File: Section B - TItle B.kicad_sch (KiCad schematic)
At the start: 12 parts, among them J2 CE, J3 Conn_01x03_Pin, U2 TLV73333PDBV, U3 MSPM0C1104SDSGR

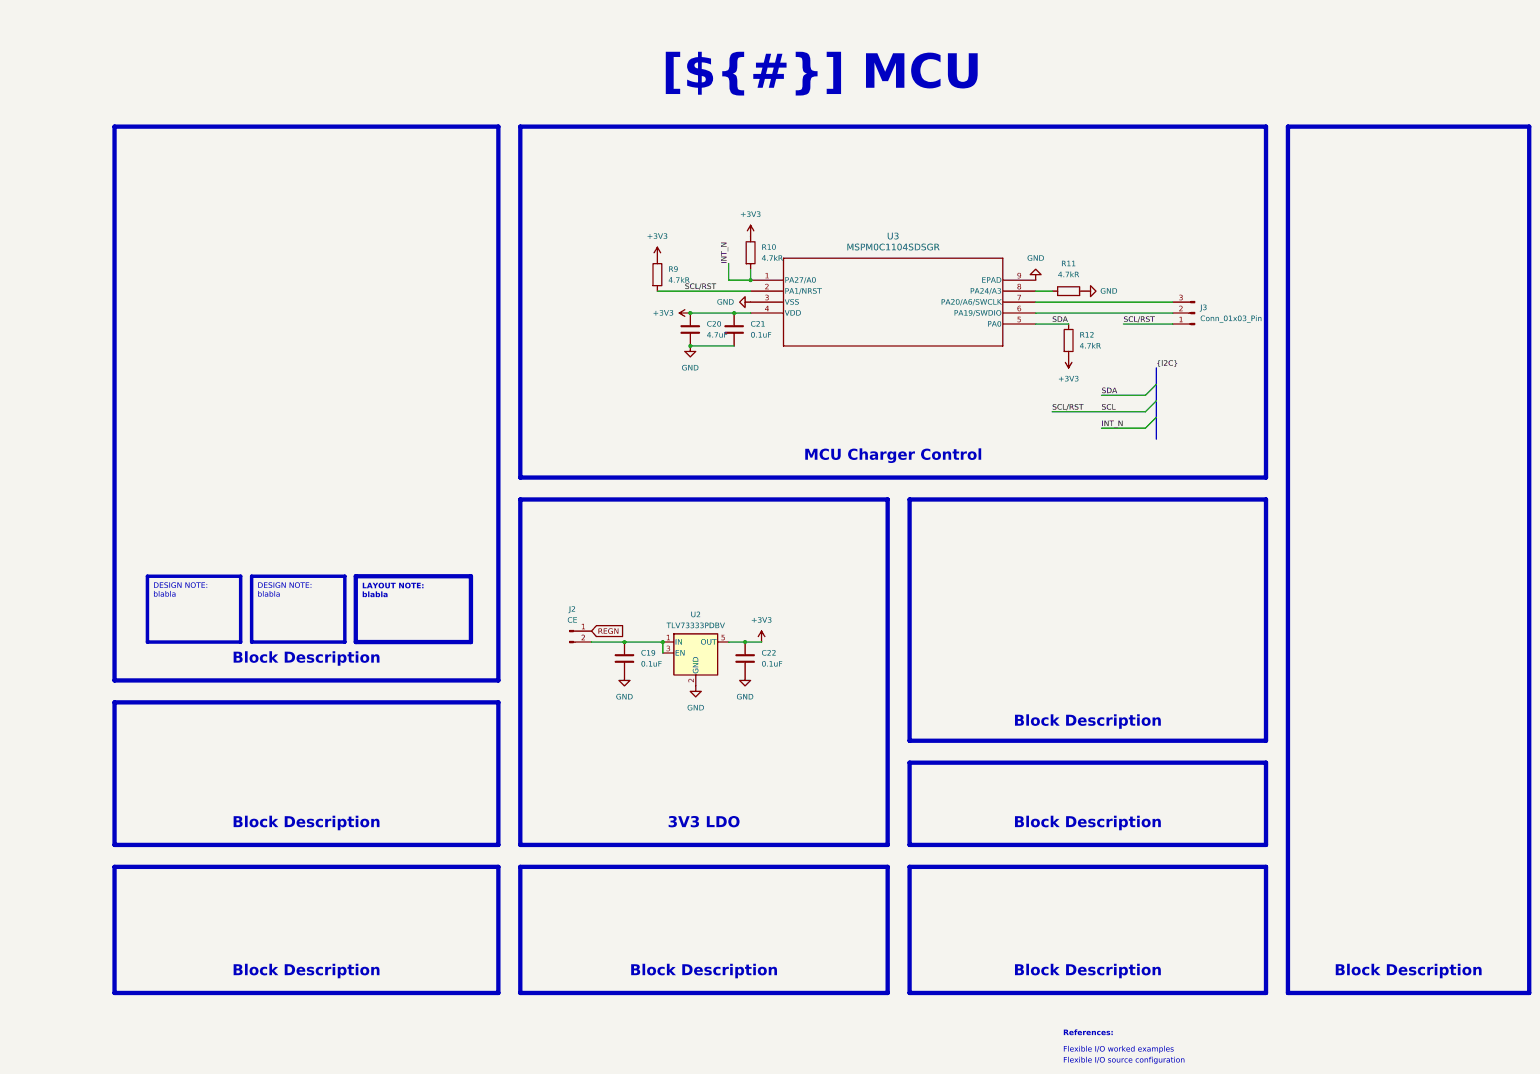
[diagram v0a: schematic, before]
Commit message: Change schematic sheet size to A4
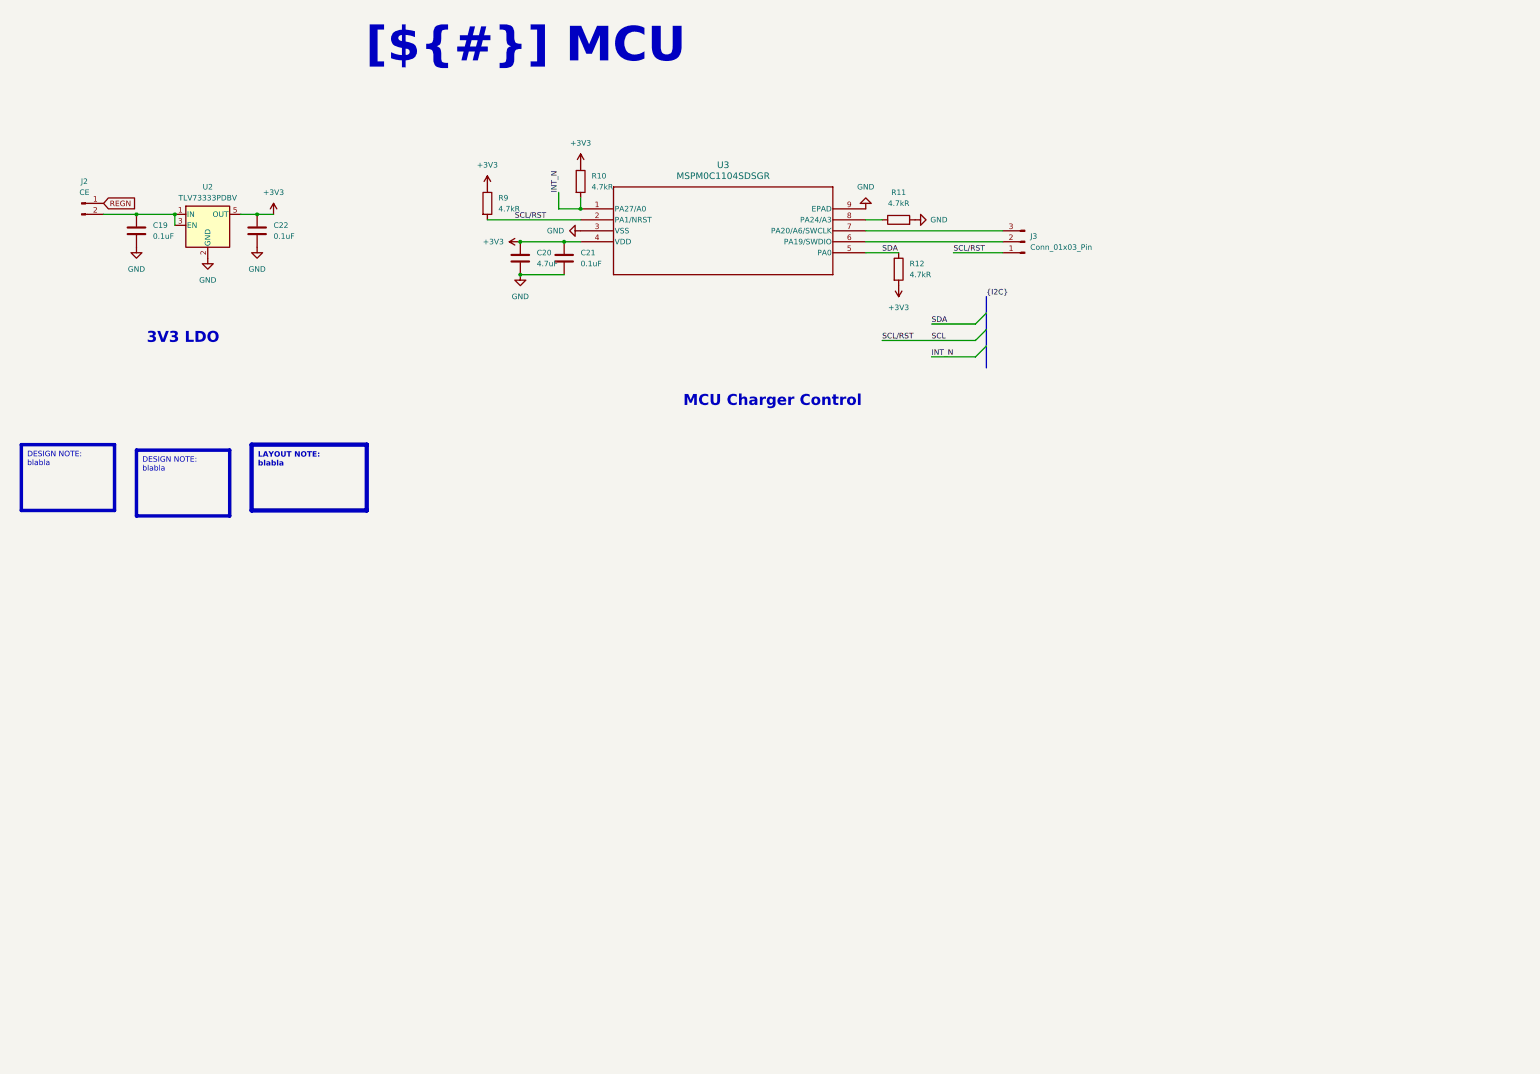
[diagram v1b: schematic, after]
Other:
- note removed: "Flexible I/O source configuration"
- note removed: "Flexible I/O worked examples"
- note removed: "References:"
- moved on the sheet: C19, C20, C21, C22, J2, J3, R10, R11, R12, R9, U2, U3

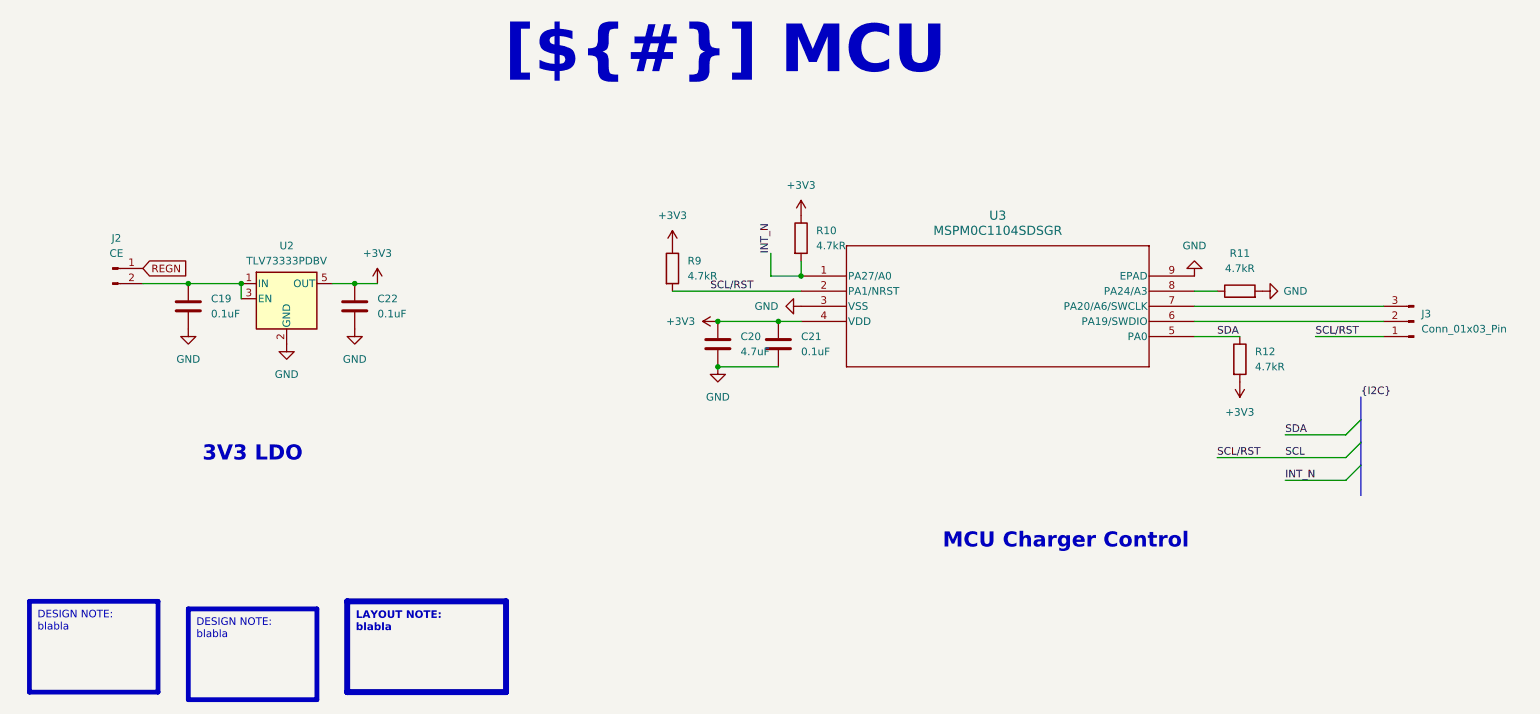
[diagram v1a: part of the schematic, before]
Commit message: Finish schematic
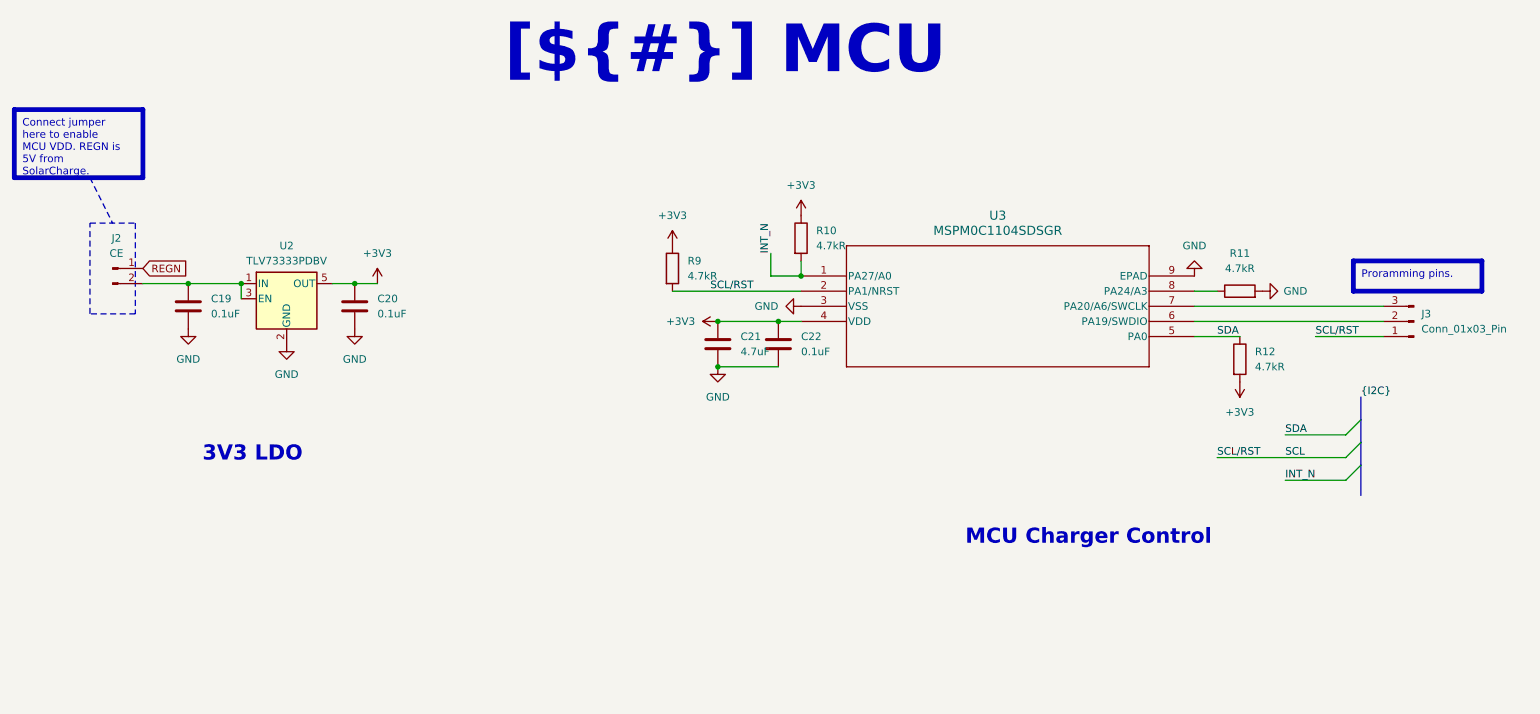
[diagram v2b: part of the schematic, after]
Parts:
- renumbered C22 to C20, C20 to C21, C21 to C22
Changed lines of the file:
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@@
 		(company "${COMPANY}")
+	)
+	(rectangle
+		(start 34.29 49.53)
+		(end 41.91 64.77)
+		(stroke
+			(width 0)
+			(type dot)
+			(color 255 0 0 1)
+		)
+		(fill
+			(type none)
+		)
+	)
+	(text_box "Connect jumper here to enable MCU VDD. REGN is 5V from SolarCharge."
+		(exclude_from_sim no)
+		(at 21.59 30.48 0)
+		(size 21.59 11.43)
+		(margins 1.3525 1.3525 1.3525 1.3525)
+		(stroke
+			(width 0.8)
+			(type solid)
+			(color 250 236 0 1)
+		)
+		(fill
+			(type none)
+		)
+		(effects
+			(font
+				(face "Arial")
+				(size 1.27 1.27)
+				(color 0 0 0 1)
+			)
+			(justify left top)
+		)
 	)
 	(text_box "[${#}] ${TITLE}"
@@
 		)
 	)
-	(text_box "DESIGN NOTE:\nblabla"
-		(exclude_from_sim no)
-		(at 50.8 114.3 0)
-		(size 21.59 15.24)
-		(margins 1.3525 1.3525 1.3525 1.3525)
-		(stroke
-			(width 0.8)
-			(type solid)
-			(color 255 165 0 1)
-		)
-		(fill
-			(type none)
-		)
-		(effects
-			(font
-				(face "Arial")
-				(size 1.27 1.27)
-				(color 0 0 0 1)
-			)
-			(justify left top)
-		)
-	)
-	(text_box "LAYOUT NOTE:\nblabla"
-		(exclude_from_sim no)
-		(at 77.47 113.03 0)
-		(size 26.67 15.24)
-		(margins 1.4525 1.4525 1.4525 1.4525)
-		(stroke
-			(width 1)
-			(type solid)
-			(color 0 0 255 1)
-		)
-		(fill
-			(type none)
-		)
-		(effects
-			(font
-				(face "Arial")
-				(size 1.27 1.27)
-				(thickness 0.4)
-				(bold yes)
-				(color 0 0 255 1)
-			)
-			(justify left top)
-		)
-	)
 	(text_box "MCU Charger Control"
 		(exclude_from_sim no)
-		(at 114.3 96.52 0)
-		(size 167.64 9.525)
+		(at 124.46 95.885 0)
+		(size 154.94 9.525)
 		(margins 1.9049 1.9049 1.9049 1.9049)
 		(stroke
@@
 		)
 	)
-	(text_box "DESIGN NOTE:\nblabla"
-		(exclude_from_sim no)
-		(at 24.13 113.03 0)
-		(size 21.59 15.24)
-		(margins 1.3525 1.3525 1.3525 1.3525)
-		(stroke
-			(width 0.8)
-			(type solid)
-			(color 200 200 200 1)
-		)
-		(fill
-			(type none)
-		)
-		(effects
-			(font
-				(face "Arial")
-				(size 1.27 1.27)
-				(color 0 0 0 1)
-			)
-			(justify left top)
-		)
-	)
 	(text_box "3V3 LDO"
 		(exclude_from_sim no)
@@
 		)
 	)
+	(text_box "Proramming pins."
+		(exclude_from_sim no)
+		(at 246.38 55.88 0)
+		(size 21.59 5.08)
+		(margins 1.3525 1.3525 1.3525 1.3525)
+		(stroke
+			(width 0.8)
+			(type solid)
+			(color 250 236 0 1)
+		)
+		(fill
+			(type none)
+		)
+		(effects
+			(font
+				(face "Arial")
+				(size 1.27 1.27)
+				(color 0 0 0 1)
+			)
+			(justify left top)
+		)
+	)
 	(junction
 		(at 78.74 59.69)
@@
 			(width 0)
 			(type default)
+		)
+	)
+	(polyline
+		(pts
+			(xy 34.29 41.91) (xy 38.1 49.53)
+		)
+		(stroke
+			(width 0)
+			(type dot)
+			(color 255 0 0 1)
 		)
 	)
@@
 		(dnp no)
 		(fields_autoplaced yes)
-		(property "Reference" "#PWR020"
+		(property "Reference" "#PWR023"
 			(at 139.7 80.01 0)
 			(effects
@@
 			(project "solar_smart_station"
 				(path "/f9e05184-c88b-4a88-ae9c-ab2bdb32be7c/c5103ceb-5325-4a84-a025-9638a412984e/e744f3ce-03a6-44a6-8792-1447ef232b9a"
-					(reference "#PWR020")
+					(reference "#PWR023")
 					(unit 1)
 				)
@@
 		(dnp no)
 		(fields_autoplaced yes)
-		(property "Reference" "C21"
+		(property "Reference" "C22"
 			(at 153.67 68.5799 0)
 			(effects
@@
 			(project "solar_smart_station"
 				(path "/f9e05184-c88b-4a88-ae9c-ab2bdb32be7c/c5103ceb-5325-4a84-a025-9638a412984e/e744f3ce-03a6-44a6-8792-1447ef232b9a"
-					(reference "C21")
+					(reference "C22")
 					(unit 1)
 				)
@@
 		(dnp no)
 		(fields_autoplaced yes)
-		(property "Reference" "#PWR025"
+		(property "Reference" "#PWR020"
 			(at 82.55 63.5 0)
 			(effects
@@
 			(project "solar_smart_station"
 				(path "/f9e05184-c88b-4a88-ae9c-ab2bdb32be7c/c5103ceb-5325-4a84-a025-9638a412984e/e744f3ce-03a6-44a6-8792-1447ef232b9a"
-					(reference "#PWR025")
+					(reference "#PWR020")
 					(unit 1)
 				)
@@
 		(dnp no)
 		(fields_autoplaced yes)
-		(property "Reference" "#PWR024"
+		(property "Reference" "#PWR025"
 			(at 147.32 63.5 0)
 			(effects
@@
 			(project "solar_smart_station"
 				(path "/f9e05184-c88b-4a88-ae9c-ab2bdb32be7c/c5103ceb-5325-4a84-a025-9638a412984e/e744f3ce-03a6-44a6-8792-1447ef232b9a"
-					(reference "#PWR024")
+					(reference "#PWR025")
 					(unit 1)
 				)
@@
 		(dnp no)
 		(fields_autoplaced yes)
-		(property "Reference" "#PWR023"
+		(property "Reference" "#PWR024"
 			(at 153.67 52.07 0)
 			(effects
@@
 			(project "solar_smart_station"
 				(path "/f9e05184-c88b-4a88-ae9c-ab2bdb32be7c/c5103ceb-5325-4a84-a025-9638a412984e/e744f3ce-03a6-44a6-8792-1447ef232b9a"
-					(reference "#PWR023")
+					(reference "#PWR024")
 					(unit 1)
 				)
@@
 		(dnp no)
 		(fields_autoplaced yes)
-		(property "Reference" "#PWR019"
+		(property "Reference" "#PWR022"
 			(at 143.51 66.04 0)
 			(effects
@@
 			(project "solar_smart_station"
 				(path "/f9e05184-c88b-4a88-ae9c-ab2bdb32be7c/c5103ceb-5325-4a84-a025-9638a412984e/e744f3ce-03a6-44a6-8792-1447ef232b9a"
-					(reference "#PWR019")
+					(reference "#PWR022")
 					(unit 1)
 				)
@@
 		(dnp no)
 		(fields_autoplaced yes)
-		(property "Reference" "#PWR022"
+		(property "Reference" "#PWR019"
 			(at 78.74 73.66 0)
 			(effects
@@
 			(project "solar_smart_station"
 				(path "/f9e05184-c88b-4a88-ae9c-ab2bdb32be7c/c5103ceb-5325-4a84-a025-9638a412984e/e744f3ce-03a6-44a6-8792-1447ef232b9a"
-					(reference "#PWR022")
+					(reference "#PWR019")
 					(unit 1)
 				)
@@
 		(dnp no)
 		(fields_autoplaced yes)
-		(property "Reference" "#PWR021"
+		(property "Reference" "#PWR018"
 			(at 67.31 76.2 0)
 			(effects
@@
 			(project "solar_smart_station"
 				(path "/f9e05184-c88b-4a88-ae9c-ab2bdb32be7c/c5103ceb-5325-4a84-a025-9638a412984e/e744f3ce-03a6-44a6-8792-1447ef232b9a"
-					(reference "#PWR021")
+					(reference "#PWR018")
 					(unit 1)
 				)
@@
 		(dnp no)
 		(fields_autoplaced yes)
-		(property "Reference" "C20"
+		(property "Reference" "C21"
 			(at 143.51 68.5799 0)
 			(effects
@@
 			(project "solar_smart_station"
 				(path "/f9e05184-c88b-4a88-ae9c-ab2bdb32be7c/c5103ceb-5325-4a84-a025-9638a412984e/e744f3ce-03a6-44a6-8792-1447ef232b9a"
-					(reference "C20")
+					(reference "C21")
 					(unit 1)
 				)
@@
 		(dnp no)
 		(fields_autoplaced yes)
-		(property "Reference" "#PWR018"
+		(property "Reference" "#PWR021"
 			(at 132.08 57.15 0)
 			(effects
@@
 			(project "solar_smart_station"
 				(path "/f9e05184-c88b-4a88-ae9c-ab2bdb32be7c/c5103ceb-5325-4a84-a025-9638a412984e/e744f3ce-03a6-44a6-8792-1447ef232b9a"
-					(reference "#PWR018")
+					(reference "#PWR021")
 					(unit 1)
 				)
@@
 		(dnp no)
 		(fields_autoplaced yes)
-		(property "Reference" "C22"
+		(property "Reference" "C20"
 			(at 82.55 62.2299 0)
 			(effects
@@
 			(project "solar_smart_station"
 				(path "/f9e05184-c88b-4a88-ae9c-ab2bdb32be7c/c5103ceb-5325-4a84-a025-9638a412984e/e744f3ce-03a6-44a6-8792-1447ef232b9a"
-					(reference "C22")
-					(unit 1)
-				)
+					(reference "C20")
+					(unit 1)
+				)

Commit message: First layout
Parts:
- removed J2: CE, Connector_PinHeader_2.54mm:PinHeader_1x02_P2.54mm_Vertical, symbol Connector:Conn_01x02_Pin
- removed J3: Conn_01x03_Pin, Connector_PinSocket_2.54mm:PinSocket_1x03_P2.54mm_Vertical, symbol Connector:Conn_01x03_Pin
- added NT1: NetTie_3, NetTie:NetTie-3_SMD_Pad0.5mm, symbol Device:NetTie_3
- added NT2: NetTie_2, NetTie:NetTie-2_SMD_Pad0.5mm, symbol Device:NetTie_2
- U3: footprint Package_TO_SOT_SMD:TSOT-23-8 -> solar_station:TSOT-23-8-shrink
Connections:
- net +3V3: now also NT2.1
- net GND: no longer U3.9 (EPAD)
- net SCL: now also NT1.1; no longer R9.2, U3.2 (PA1/NRST)
- net LDO_IN: now reaches C19.2, U2.1 (IN), U2.3 (EN)
- net SWDIO: now reaches U3.6 (PA19/SWDIO)
- net SWCLK: now reaches U3.7 (PA20/A6/SWCLK)
- new net RST: NT1.3
- new net SCL/RST: NT1.2, R9.2, U3.2 (PA1/NRST)
- new net VCC: NT2.2
